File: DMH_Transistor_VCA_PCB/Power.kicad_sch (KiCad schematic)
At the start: 14 parts, among them J0 Conn_01x01, J100 IDC_02x05, J101 IDC_02x08

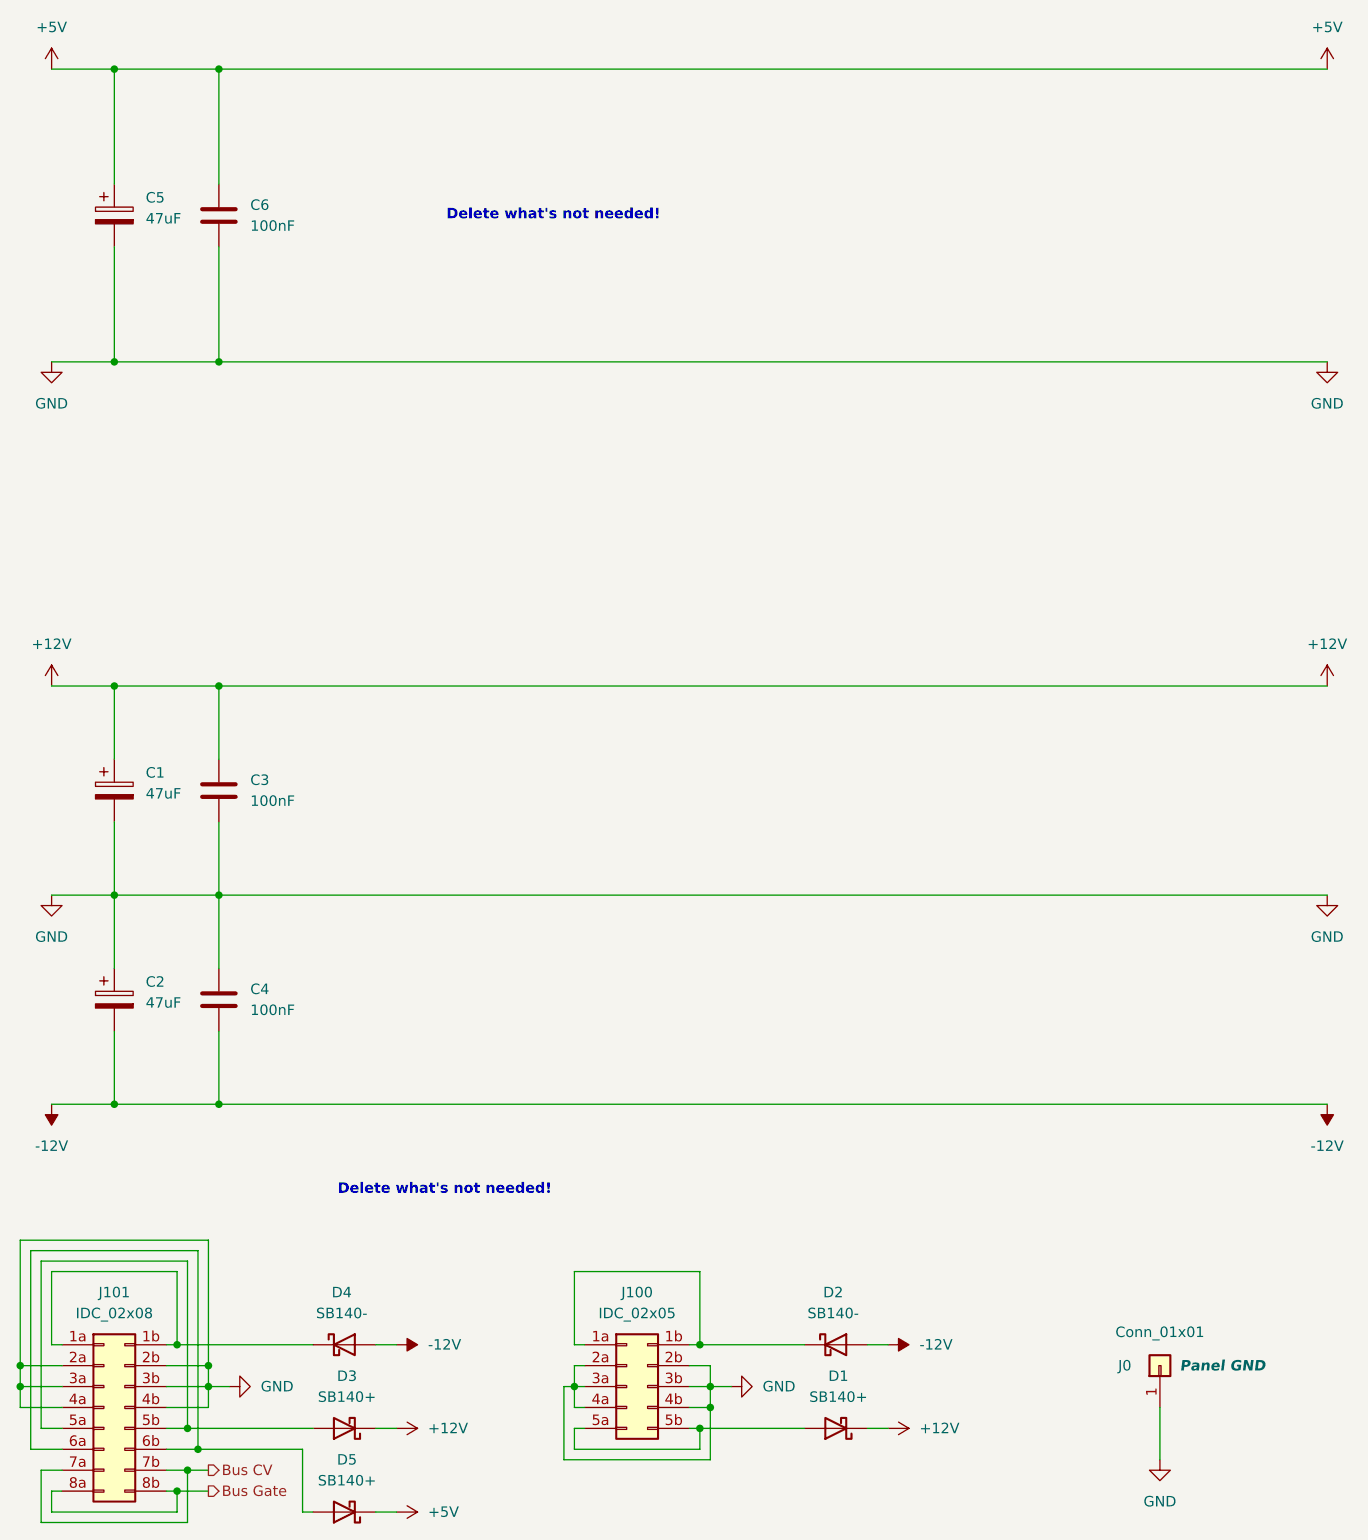
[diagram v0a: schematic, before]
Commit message: Finished core circuit schematic
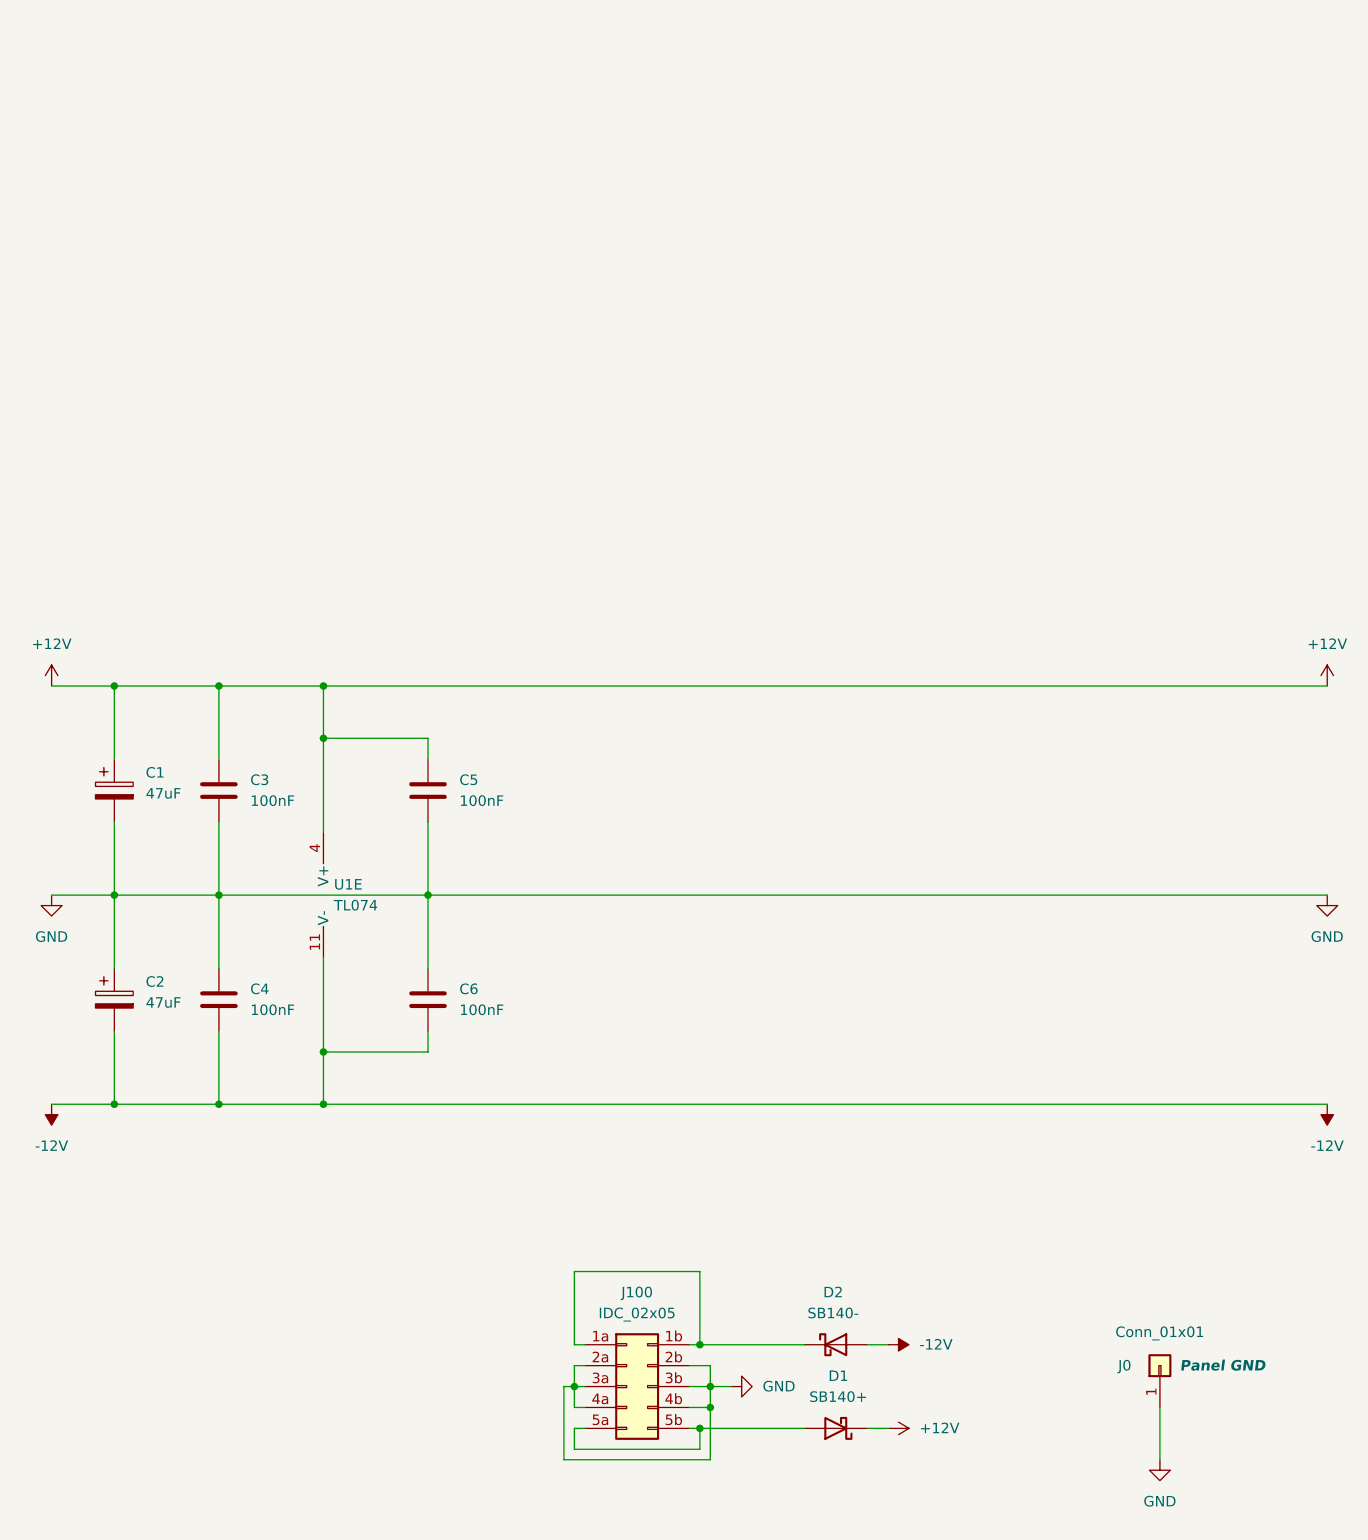
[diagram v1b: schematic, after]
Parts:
- removed C5: 47uF, Capacitor_THT:CP_Radial_D4.0mm_P1.50mm, symbol Device:C_Polarized
- removed D3, D5: SB140+, Diode_THT:D_DO-41_SOD81_P10.16mm_Horizontal, symbol SynthStuff:Power_Bus_Schotty_+
- removed D4: SB140-, Diode_THT:D_DO-41_SOD81_P10.16mm_Horizontal, symbol SynthStuff:Power_Bus_Schotty_-
- removed J101: IDC_02x08, SynthStuff:IDC-Header_2x08_P2.54mm_Vertical_Eurorack, symbol SynthStuff:Eurorack_Power_Connector_16Pin
- added C5: 100nF, Capacitor_THT:C_Disc_D4.3mm_W1.9mm_P5.00mm, symbol Device:C
- added U1: TL074, Package_DIP:DIP-14_W7.62mm_Socket, symbol Amplifier_Operational:TL074
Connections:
- net +5V is gone; now on net GND: C6.1
- net +12V: now also C5.1, U1.4 (V+)
- net -12V: now also C6.2, U1.11 (V-)
- net GND: now also C5.2; no longer C6.2
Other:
- note removed: "Delete what's not needed!"

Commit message: Finished schematic
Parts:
- added C7, C8: 100nF, Capacitor_THT:C_Disc_D4.3mm_W1.9mm_P5.00mm, symbol Device:C
- added U2: TL074, symbol Amplifier_Operational:TL074
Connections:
- net +12V: now also C7.1, U2.4 (V+)
- net -12V: now also C8.2, U2.11 (V-)
- net GND: now also C7.2, C8.1

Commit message: Finished main PCB
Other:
- note added: "Pots PCB"
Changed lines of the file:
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@@
+		)
+	)
+	(rectangle
+		(start 138.43 168.91)
+		(end 166.37 196.85)
+		(stroke
+			(width 0)
+			(type default)
+		)
+		(fill
+			(type none)
+		)
+	)
+	(text "Pots PCB"
+		(exclude_from_sim no)
+		(at 143.51 195.58 0)
+		(effects
+			(font
+				(size 1.27 1.27)
+			)
 		)
 	)
@@
 		(exclude_from_sim no)
 		(in_bom yes)
-		(on_board yes)
+		(on_board no)
 		(dnp no)
 		(property "Reference" "J0"

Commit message: Pots PCB in progress
Need to add CV input traces to the pin headers
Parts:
- removed J0: Conn_01x01, Connector_PinHeader_2.54mm:PinHeader_1x01_P2.54mm_Vertical, symbol Connector_Generic:Conn_01x01
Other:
- note removed: "Pots PCB"
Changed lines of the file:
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@@
-	(wire
-		(pts
-			(xy 152.4 182.88) (xy 152.4 189.23)
-		)
-		(stroke
-			(width 0)
-			(type default)
-		)
-	)
 	(wire
 		(pts
@@
 			(width 0)
 			(type default)
-		)
-	)
-	(rectangle
-		(start 138.43 168.91)
-		(end 166.37 196.85)
-		(stroke
-			(width 0)
-			(type default)
-		)
-		(fill
-			(type none)
-		)
-	)
-	(text "Pots PCB"
-		(exclude_from_sim no)
-		(at 143.51 195.58 0)
-		(effects
-			(font
-				(size 1.27 1.27)
-			)
 		)
 	)
@@
 	)
 	(symbol
-		(lib_id "Connector_Generic:Conn_01x01")
-		(at 152.4 177.8 90)
-		(unit 1)
-		(exclude_from_sim no)
-		(in_bom yes)
-		(on_board no)
-		(dnp no)
-		(property "Reference" "J0"
-			(at 147.32 177.8 90)
-			(effects
-				(font
-					(size 1.27 1.27)
-				)
-				(justify right)
-			)
-		)
-		(property "Value" "Conn_01x01"
-			(at 152.4 173.736 90)
-			(effects
-				(font
-					(size 1.27 1.27)
-				)
-			)
-		)
-		(property "Footprint" "Connector_PinHeader_2.54mm:PinHeader_1x01_P2.54mm_Vertical"
-			(at 152.4 177.8 0)
-			(effects
-				(font
-					(size 1.27 1.27)
-				)
-				(hide yes)
-			)
-		)
-		(property "Datasheet" "~"
-			(at 152.4 177.8 0)
-			(effects
-				(font
-					(size 1.27 1.27)
-				)
-				(hide yes)
-			)
-		)
-		(property "Description" "Generic connector, single row, 01x01, script generated (kicad-library-utils/schlib/autogen/connector/)"
-			(at 152.4 177.8 0)
-			(effects
-				(font
-					(size 1.27 1.27)
-				)
-				(hide yes)
-			)
-		)
-		(property "Function" "Panel GND"
-			(at 160.02 177.8 90)
-			(effects
-				(font
-					(size 1.27 1.27)
-					(thickness 0.254)
-					(bold yes)
-					(italic yes)
-				)
-			)
-		)
-		(pin "1"
-		)
-		(instances
-			(project "DMH-Kosmo-5cm-PCB"
-				(path "/58f4306d-5387-4983-bb08-41a2313fd315/0cdf34b2-39cd-4d9e-981a-97cd34791509"
-					(reference "J0")
-					(unit 1)
-				)
-			)
-		)
-	)
-	(symbol
 		(lib_id "power:+12V")
 		(at 17.78 95.25 0)
@@
 					(unit 1)
 				)
-			)
-		)
-	)
-	(symbol
-		(lib_id "power:GND")
-		(at 152.4 189.23 0)
-		(unit 1)
-		(exclude_from_sim no)
-		(in_bom yes)
-		(on_board yes)
-		(dnp no)
-		(fields_autoplaced yes)
-		(property "Reference" "#PWR08"
-			(at 152.4 195.58 0)
-			(effects
-				(font
-					(size 1.27 1.27)
-				)
-				(hide yes)
-			)
-		)
-		(property "Value" "GND"
-			(at 152.4 194.31 0)
-			(effects
-				(font
-					(size 1.27 1.27)
-				)
-			)
-		)
-		(property "Footprint" ""
-			(at 152.4 189.23 0)
-			(effects
-				(font
-					(size 1.27 1.27)
-				)
-				(hide yes)
-			)
-		)
-		(property "Datasheet" ""
-			(at 152.4 189.23 0)
-			(effects
-				(font
-					(size 1.27 1.27)
-				)
-				(hide yes)
-			)
-		)
-		(property "Description" "Power symbol creates a global label with name \"GND\" , ground"
-			(at 152.4 189.23 0)
-			(effects
-				(font
-					(size 1.27 1.27)
-				)
-				(hide yes)
-			)
-		)
-		(pin "1"
-		)
-		(instances
-			(project "DMH-Kosmo-5cm-PCB"
-				(path "/58f4306d-5387-4983-bb08-41a2313fd315/0cdf34b2-39cd-4d9e-981a-97cd34791509"
-					(reference "#PWR08")
-					(unit 1)
-				)
